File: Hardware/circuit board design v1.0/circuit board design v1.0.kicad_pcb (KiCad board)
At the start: 2 copper layers, 2 parts, among them U1 STM32F303RCTx, U2 MAX-M8Q

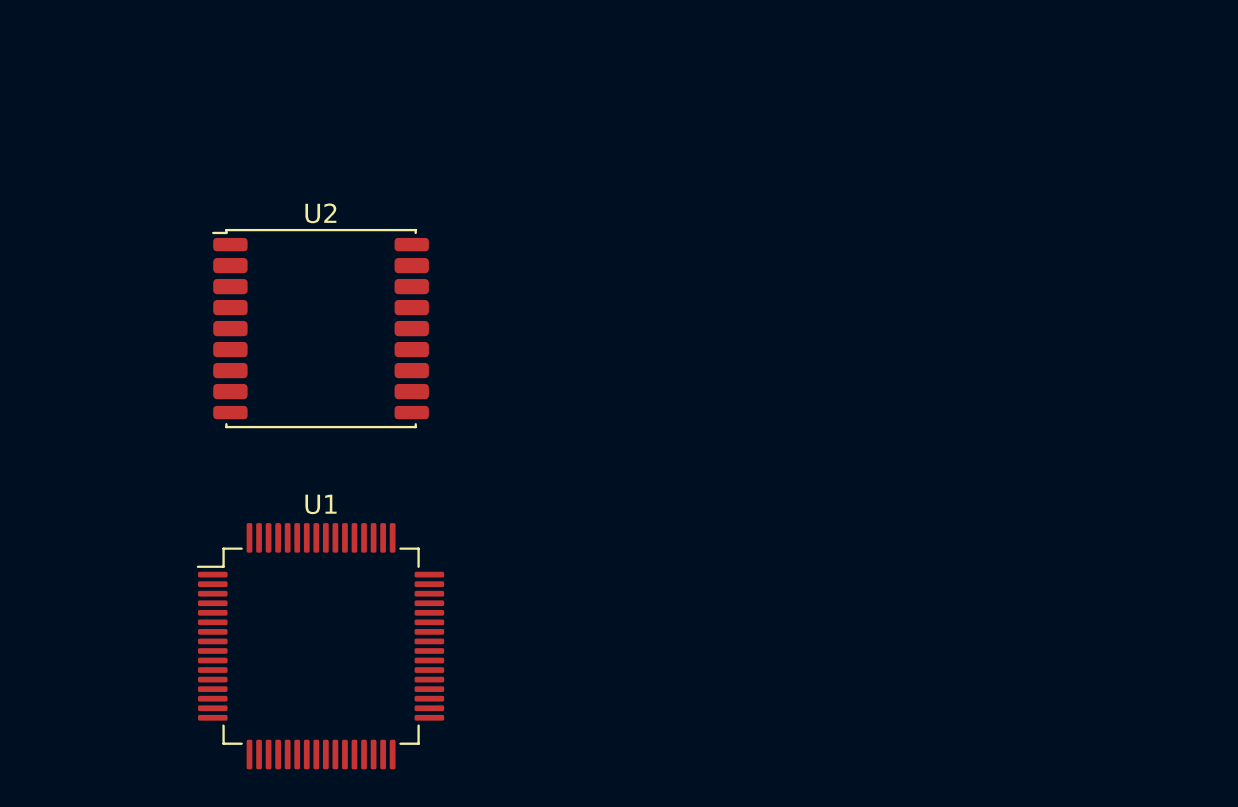
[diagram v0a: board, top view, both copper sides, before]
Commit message: BMI088 schematic
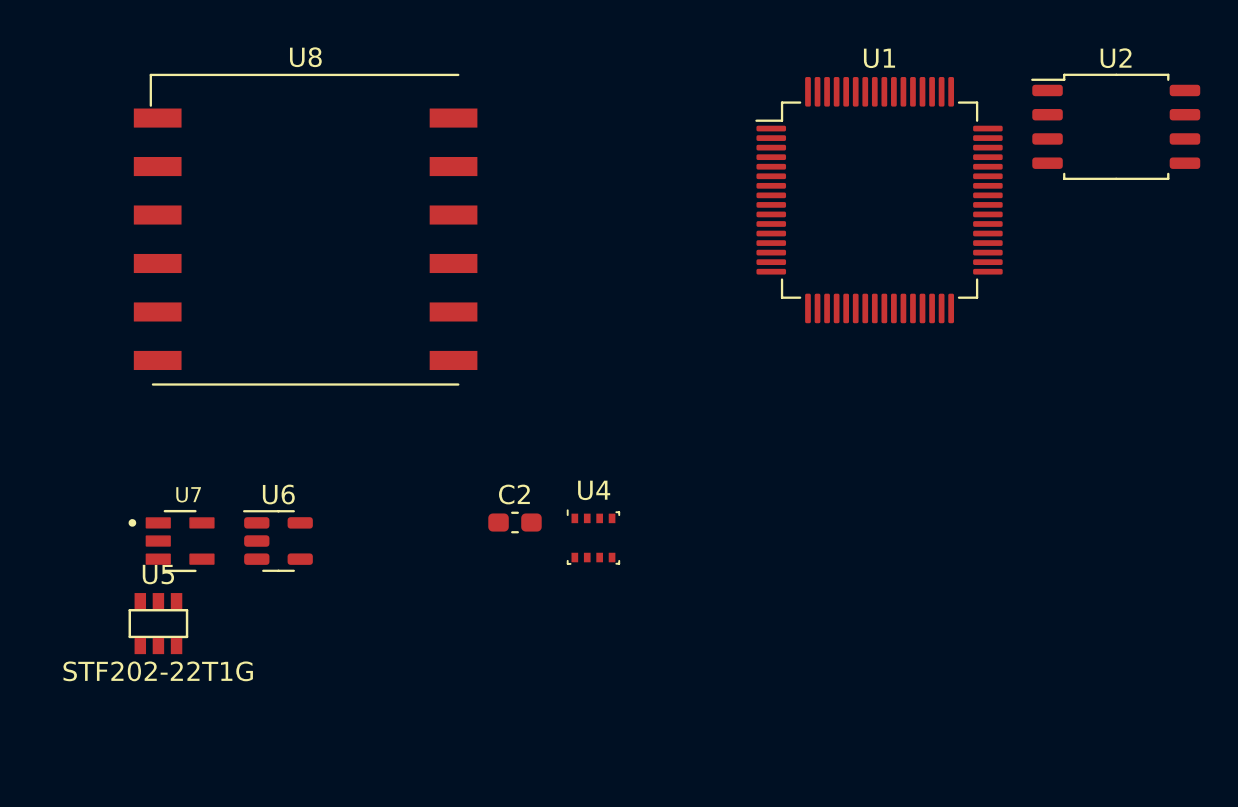
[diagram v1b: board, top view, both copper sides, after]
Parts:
- added C2: 100n, Capacitor_SMD:C_0603_1608Metric_Pad1.08x0.95mm_HandSolder, F.Cu at (152.4, 81.3)
- added U4: BME280, Package_LGA:Bosch_LGA-8_2.5x2.5mm_P0.65mm_ClockwisePinNumbering, F.Cu at (156.5, 82.1)
- added U5: STF202-22T1G, Components:STF202-22T1G, F.Cu at (133.7, 86.6)
- added U6: MAX40203_SOT23, Package_TO_SOT_SMD:SOT-23-5, F.Cu at (140.0, 82.2)
- added U7: NCP161ASN180T1G, Components:SOT95P280X145-5N, F.Cu at (134.9, 82.2)
- added U8: L80-R, RF_GPS:Quectel_L80-R, F.Cu at (141.4, 65.9)
- U1: value STM32F303RCTx -> STM32F446RETx
- U2: value MAX-M8Q -> W25Q64JVSS; footprint RF_GPS:ublox_MAX -> Package_SO:SOIC-8_5.23x5.23mm_P1.27mm
- moved U2 43.0 mm to (183.9, 60.5)
- moved U1 37.4 mm to (171.5, 64.4)
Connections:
- U1 pad 42: /GPS/GPS_NSAFEBOOT -> unconnected-(U1-Pad42)
- U1 pad 43: /GPS/GPS_1PPS -> unconnected-(U1-Pad43)
- U1 pad 44: /GPS/GPS_NRES -> unconnected-(U1-Pad44)
- U1 pad 45: /GPS/GPS_RXD -> unconnected-(U1-Pad45)
- U1 pad 46: /GPS/GPS_TXD -> unconnected-(U1-Pad46)
- U1 pad 49: /GPS/GPS_SDA -> unconnected-(U1-Pad49)
- U1 pad 50: /GPS/GPS_SCL -> unconnected-(U1-Pad50)
- U2 pad 1: GND -> unconnected-(U2-Pad1)
- U2 pad 2: /GPS/GPS_TXD -> unconnected-(U2-Pad2)
- U2 pad 3: /GPS/GPS_RXD -> unconnected-(U2-Pad3)
- U2 pad 4: /GPS/GPS_1PPS -> unconnected-(U2-Pad4)
- U2 pad 6: +3.3V -> unconnected-(U2-Pad6)
- U2 pad 7: +3.3V -> unconnected-(U2-Pad7)
- U2 pad 8: +3.3V -> unconnected-(U2-Pad8)

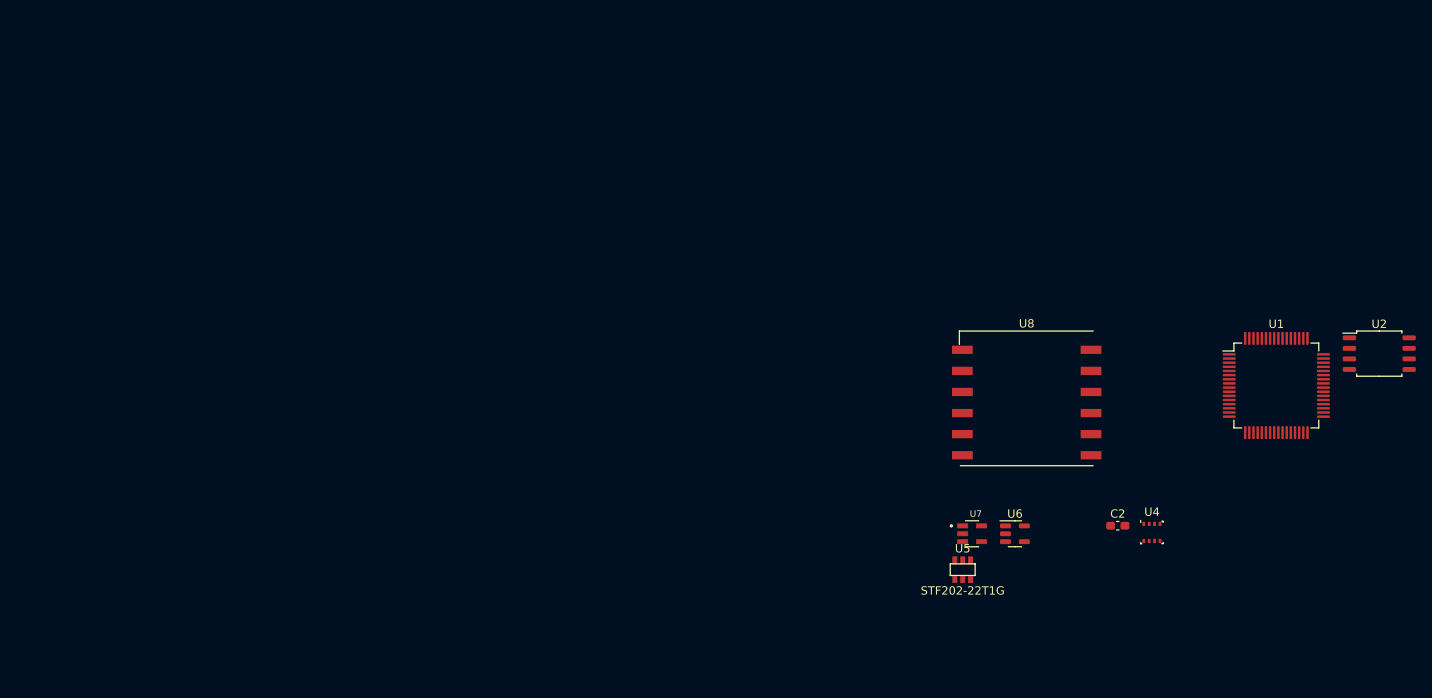
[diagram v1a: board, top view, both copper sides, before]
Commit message: Created stm32mx project and started on layout
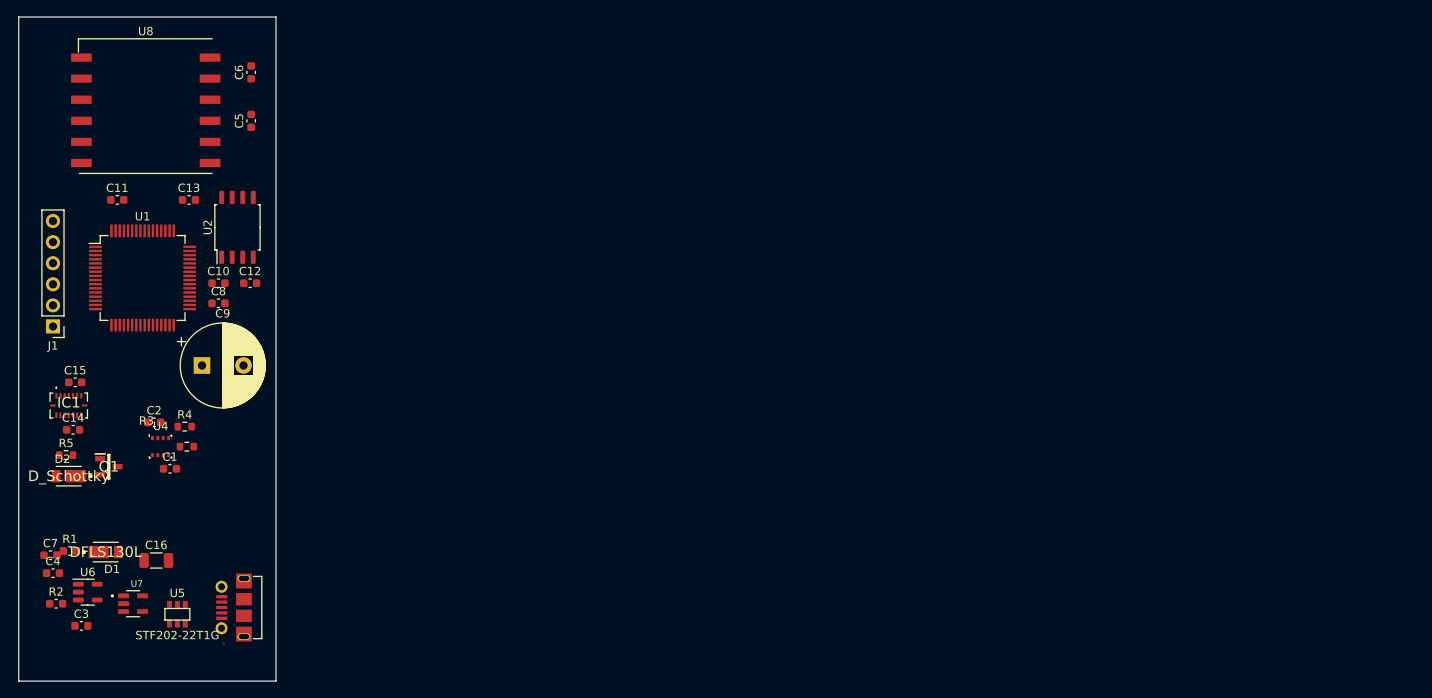
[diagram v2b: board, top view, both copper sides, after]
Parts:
- added C1: 100n, Capacitor_SMD:C_0603_1608Metric, F.Cu at (38.2, 74.4)
- added C10: 100n, Capacitor_SMD:C_0603_1608Metric, F.Cu at (44.1, 52.1)
- added C11: 100n, Capacitor_SMD:C_0603_1608Metric, F.Cu at (31.9, 42.0)
- added C12: 100n, Capacitor_SMD:C_0603_1608Metric, F.Cu at (47.9, 52.1)
- added C13: 100n, Capacitor_SMD:C_0603_1608Metric, F.Cu at (40.5, 42.0)
- added C14: C_Small, Capacitor_SMD:C_0603_1608Metric, F.Cu at (26.6, 69.7)
- added C15: C_Small, Capacitor_SMD:C_0603_1608Metric, F.Cu at (26.8, 64.0)
- added C16: 1uF, Capacitor_SMD:C_1206_3216Metric, F.Cu at (36.6, 85.5)
- added C3: C_Small, Capacitor_SMD:C_0603_1608Metric, F.Cu at (27.6, 93.3)
- added C4: C_Small, Capacitor_SMD:C_0603_1608Metric, F.Cu at (24.1, 87.0)
- added C5: 100n, Capacitor_SMD:C_0603_1608Metric, F.Cu at (48.0, 32.5)
- added C6: C_Small, Capacitor_SMD:C_0603_1608Metric, F.Cu at (48.0, 26.7)
- added C7: 100n, Capacitor_SMD:C_0603_1608Metric, F.Cu at (23.8, 84.8)
- added C8: 100n, Capacitor_SMD:C_0603_1608Metric, F.Cu at (44.1, 54.5)
- added C9: 4.7u, Capacitor_THT:CP_Radial_D10.0mm_P5.00mm, F.Cu at (42.1, 62.0)
- added D1: DFLS130L, Components:PowerDI123, F.Cu at (30.5, 84.5)
- added D2: D_Schottky, Components:PowerDI123, F.Cu at (26.0, 75.3)
- added IC1: BMI088, Components:BMI088, F.Cu at (26.0, 66.8)
- added J1: Conn_01x06_Male, Connector_PinHeader_2.54mm:PinHeader_1x06_P2.54mm_Vertical, F.Cu at (24.1, 57.3)
- added J3: 105017-0001, Components:MOLEX_105017-0001, F.Cu at (47.1, 91.1)
- added Q1: 2N7002-7-F, Components:SOT96P240X120-3N, F.Cu at (30.9, 74.2)
- added R1: R, Capacitor_SMD:C_0603_1608Metric, F.Cu at (26.2, 84.3)
- added R2: R, Capacitor_SMD:C_0603_1608Metric, F.Cu at (24.5, 90.7)
- added R3: 4.7k, Resistor_SMD:R_0603_1608Metric, F.Cu at (40.3, 71.8)
- added R4: 4.7k, Resistor_SMD:R_0603_1608Metric, F.Cu at (40.0, 69.3)
- added R5: 68, Resistor_SMD:R_0603_1608Metric, F.Cu at (25.7, 72.8)
- C2: footprint Capacitor_SMD:C_0603_1608Metric_Pad1.08x0.95mm_HandSolder -> Capacitor_SMD:C_0603_1608Metric
- U8: footprint RF_GPS:Quectel_L80-R -> Components:Quectel_L80-R
- moved U2 138.4 mm to (46.4, 45.3), turned to 90 degrees
- moved U1 137.2 mm to (34.9, 51.4)
- moved U4 119.9 mm to (37.1, 71.8)
- moved C2 116.7 mm to (36.3, 68.8)
- moved U6 111.9 mm to (28.3, 89.3)
- moved U8 111.8 mm to (35.3, 30.7)
- moved U7 101.4 mm to (33.8, 90.7)
- moved U5 94.8 mm to (39.1, 91.9)
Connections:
- U1 pad 12: unconnected-(U1-Pad12) -> GND
- U1 pad 13: unconnected-(U1-Pad13) -> +3.3VA
- U1 pad 14: unconnected-(U1-Pad14) -> /GPS/rx_gps
- U1 pad 15: unconnected-(U1-Pad15) -> /GPS/tx_gps
- U1 pad 17: unconnected-(U1-Pad17) -> /MCU/buzzer_gate
- U1 pad 18: unconnected-(U1-Pad18) -> GND
- U1 pad 19: unconnected-(U1-Pad19) -> +3.3V
- U1 pad 28: unconnected-(U1-Pad28) -> /MCU/QUADSPI_CLK
- U1 pad 30: unconnected-(U1-Pad30) -> Net-(C9-Pad1)
- U1 pad 31: unconnected-(U1-Pad31) -> GND
- U1 pad 32: unconnected-(U1-Pad32) -> +3.3V
- U1 pad 40: unconnected-(U1-Pad40) -> /MCU/QUADSPI_IO0
- U1 pad 44: unconnected-(U1-Pad44) -> /MCU/usb_dm
- U1 pad 45: unconnected-(U1-Pad45) -> /MCU/usb_dp
- U1 pad 46: unconnected-(U1-Pad46) -> /MCU/SYS_JTMS-SWDIO
- U1 pad 47: unconnected-(U1-Pad47) -> GND
- U1 pad 48: unconnected-(U1-Pad48) -> +3.3V
- U1 pad 49: unconnected-(U1-Pad49) -> /MCU/SYS_JTCK_SWCLK
- U1 pad 5: unconnected-(U1-Pad5) -> Net-(U1-Pad5)
- U1 pad 50: unconnected-(U1-Pad50) -> /MCU/SYS_JTDI
- U1 pad 51: unconnected-(U1-Pad51) -> /MCU/QUADSPI_IO1
- U1 pad 55: unconnected-(U1-Pad55) -> /MCU/SYS_JTRST
- U1 pad 56: unconnected-(U1-Pad56) -> /MCU/SYS_JTDO-SWO
- U1 pad 58: unconnected-(U1-Pad58) -> /MCU/QUADSPI_NCS
- U1 pad 59: unconnected-(U1-Pad59) -> /MCU/SCL
- U1 pad 6: unconnected-(U1-Pad6) -> Net-(U1-Pad6)
- U1 pad 61: unconnected-(U1-Pad61) -> /MCU/SCL
- U1 pad 63: unconnected-(U1-Pad63) -> GND
- U1 pad 64: unconnected-(U1-Pad64) -> +3.3V
- U2 pad 1: unconnected-(U2-Pad1) -> /MCU/QUADSPI_NCS
- U2 pad 2: unconnected-(U2-Pad2) -> /MCU/QUADSPI_IO1
- U2 pad 4: unconnected-(U2-Pad4) -> GND
- U2 pad 5: unconnected-(U2-Pad5) -> /MCU/QUADSPI_IO0
- U2 pad 6: unconnected-(U2-Pad6) -> /MCU/QUADSPI_CLK
- U2 pad 8: unconnected-(U2-Pad8) -> +3.3V
- U4 pad 3: /Sensors/SDA -> /MCU/SCL
- U4 pad 4: /Sensors/SDA -> /MCU/SCL
- U5 pad 2: /Power/usb_dm -> /MCU/usb_dm
- U5 pad 3: /Power/usb_db -> /MCU/usb_dp
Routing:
- added copper zone on In1.Cu, net +3.3V
- added copper zone on In2.Cu, net GND
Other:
- board outline added: 31 x 80 mm
- copper layers 2 -> 4
